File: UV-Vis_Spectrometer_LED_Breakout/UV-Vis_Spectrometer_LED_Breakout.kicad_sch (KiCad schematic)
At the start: 0 parts

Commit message: Designed adjustable LED current source
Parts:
- added C1, C2: 100nF, Capacitor_SMD:C_0603_1608Metric, symbol Device:C
- added H1, H2, H3, H4: MountingHole, Mounting_Wuerth:Mounting_Wuerth_WA-SMSI-M1.6_H4.5mm_ThreadDepth2mm_97730456332, symbol Mechanical:MountingHole
- added J1: Conn_01x02, Connector_JST:JST_EH_S2B-EH_1x02_P2.50mm_Horizontal, symbol Connector_Generic:Conn_01x02
- added Q1: BSS138, Package_TO_SOT_SMD:SOT-23, symbol Transistor_FET:BSS138
- added R1: 100, Resistor_SMD:R_0603_1608Metric, symbol Device:R_US
- added R2: 100k, Resistor_SMD:R_0603_1608Metric, symbol Device:R_US
- added R3: 10, Resistor_SMD:R_0603_1608Metric, symbol Device:R_US
- added R4: 117k, Resistor_SMD:R_0603_1608Metric, symbol Device:R_US
- added R5: 1k, Resistor_SMD:R_0603_1608Metric, symbol Device:R_US
- added RV1: 10k, Potentiometer_THT:Potentiometer_Bourns_3296W_Vertical, symbol Device:R_Potentiometer_Trim_US
- added SK1: (no value), symbol UV-Vis_Symbol_Lib:8060-2C
- added TP1: I_{Set}, TestPoint:TestPoint_Pad_D1.5mm, symbol Connector:TestPoint
- added U2: LMV321AIDCKR, Package_TO_SOT_SMD:SOT-353_SC-70-5, symbol Amplifier_Operational:LMV321
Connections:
- new net: R5.1, RV1.2
- new net: R4.1, RV1.3
- new net: C2.1, R5.2, TP1.1, U2.1 (+)
- new net: Q1.1 (G), R1.2
- new net: Q1.3 (D), SK1.2
- new net: R1.1, R2.2, U2.4
- new net +3.3V: C1.1, J1.1 (Pin_1), R4.2, SK1.1, U2.5 (V+)
- new net CS/FB: Q1.2 (S), R3.2, U2.3 (-)
- new net GND: C1.2, C2.2, J1.2 (Pin_2), R2.1, R3.1, RV1.1, U2.2 (V-)
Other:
- note added: "(0 - 264mV)"
- note added: "Current Setpoint (0 - 25mA)"
- note added: "LED Socket"
- note added: "PWR INPUT"

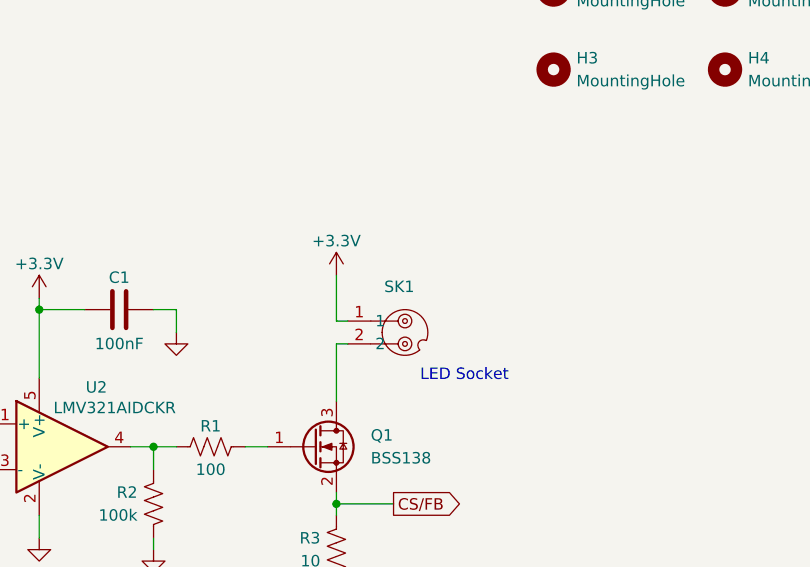
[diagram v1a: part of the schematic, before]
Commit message: Added datasheet to LED socket symbol
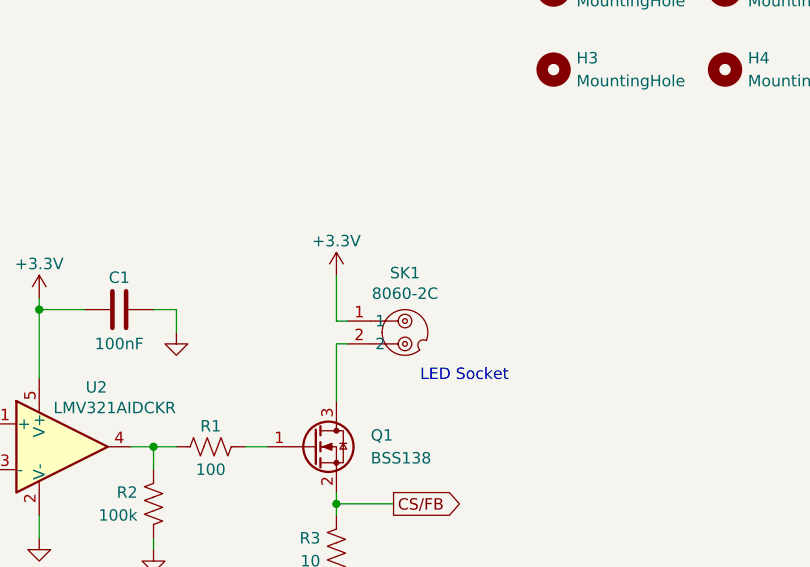
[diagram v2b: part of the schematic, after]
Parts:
- SK1: value (none) -> 8060-2C
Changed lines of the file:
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@@
 		(dnp no)
 		(property "Reference" "SK1"
-			(at 142.875 52.07 0)
+			(at 143.51 50.546 0)
 			(show_name no)
 			(do_not_autoplace no)
@@
 			)
 		)
-		(property "Value" ""
-			(at 143.51 57.15 0)
+		(property "Value" "8060-2C"
+			(at 143.51 52.832 0)
 			(show_name no)
 			(do_not_autoplace no)
@@
 			)
 		)
-		(property "Datasheet" ""
+		(property "Datasheet" "https://www.thorlabs.com/item/8060-2C"
 			(at 143.51 57.15 0)
 			(hide yes)
@@
 			)
 		)
-		(property "Description" ""
+		(property "Description" "Light-Emitting Diode Socket for LEDs, 2 Pin"
 			(at 143.51 57.15 0)
 			(hide yes)

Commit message: Added LED shunt testpoint
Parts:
- added TP2: I_{LED}, TestPoint:TestPoint_Pad_D1.5mm, symbol Connector:TestPoint
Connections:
- net CS/FB: now also TP2.1
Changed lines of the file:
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@@
+	)
+	(junction
+		(at 135.89 76.2)
+		(diameter 0)
+		(color 0 0 0 0)
 	)
 	(junction
@@
 	)
 	(junction
-		(at 135.89 76.2)
+		(at 151.13 76.2)
 		(diameter 0)
 		(color 0 0 0 0)
@@
 		)
 	)
+	(wire
+		(pts
+			(xy 151.13 76.2) (xy 154.94 76.2)
+		)
+		(stroke
+			(width 0)
+			(type default)
+		)
+	)
 	(polyline
 		(pts
@@
 	(wire
 		(pts
-			(xy 135.89 76.2) (xy 142.24 76.2)
+			(xy 135.89 76.2) (xy 151.13 76.2)
 		)
 		(stroke
@@
 		(pts
 			(xy 87.63 67.31) (xy 97.79 67.31)
+		)
+		(stroke
+			(width 0)
+			(type default)
+		)
+	)
+	(wire
+		(pts
+			(xy 151.13 71.12) (xy 151.13 76.2)
 		)
 		(stroke
@@
 	(global_label "CS{slash}FB"
 		(shape output)
-		(at 142.24 76.2 0)
+		(at 154.94 76.2 0)
 		(fields_autoplaced yes)
 		(effects
@@
 		)
 		(property "Intersheetrefs" "${INTERSHEET_REFS}"
-			(at 151.3938 76.2 0)
+			(at 164.0938 76.2 0)
 			(hide yes)
 			(show_name no)
@@
 					(unit 1)
 				)
+			)
+		)
+	)
+	(symbol
+		(lib_id "Connector:TestPoint")
+		(at 151.13 71.12 0)
+		(unit 1)
+		(body_style 1)
+		(exclude_from_sim no)
+		(in_bom yes)
+		(on_board yes)
+		(in_pos_files yes)
+		(dnp no)
+		(property "Reference" "TP2"
+			(at 153.67 66.5479 0)
+			(show_name no)
+			(do_not_autoplace no)
+			(effects
+				(font
+					(size 1.27 1.27)
+				)
+				(justify left)
+			)
+		)
+		(property "Value" "I_{LED}"
+			(at 153.67 69.0879 0)
+			(show_name no)
+			(do_not_autoplace no)
+			(effects
+				(font
+					(size 1.27 1.27)
+				)
+				(justify left)
+			)
+		)
+		(property "Footprint" "TestPoint:TestPoint_Pad_D1.5mm"
+			(at 156.21 71.12 0)
+			(hide yes)
+			(show_name no)
+			(do_not_autoplace no)
+			(effects
+				(font
+					(size 1.27 1.27)
+				)
+			)
+		)
+		(property "Datasheet" ""
+			(at 156.21 71.12 0)
+			(hide yes)
+			(show_name no)
+			(do_not_autoplace no)
+			(effects
+				(font
+					(size 1.27 1.27)
+				)
+			)
+		)
+		(property "Description" "test point"
+			(at 151.13 71.12 0)
+			(hide yes)
+			(show_name no)
+			(do_not_autoplace no)
+			(effects
+				(font
+					(size 1.27 1.27)
+				)
+			)
+		)
+		(pin "1"
+		)
+		(instances
+			(project "UV-Vis_Spectrometer_LED_Breakout"
+				(path "/5c1f1d7c-1e3d-4eca-b2bd-28e8cad4d986"
+					(reference "TP2")
+					(unit 1)
+				)

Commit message: Made layout for LED driver.
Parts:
- SK1: footprint (none) -> UV_LED_Socket:8060-2C
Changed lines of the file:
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@@
 			)
 		)
-		(property "Footprint" ""
+		(property "Footprint" "UV_LED_Socket:8060-2C"
 			(at 143.51 57.15 0)
 			(hide yes)
